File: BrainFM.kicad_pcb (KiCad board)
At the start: 2 copper layers, 21 x 34.3 mm, 18 parts, among them J1 USB_B_Micro, U1 PAM8302AAD, U2 MCP73831-2-OT, U3 TLV75801PDBV

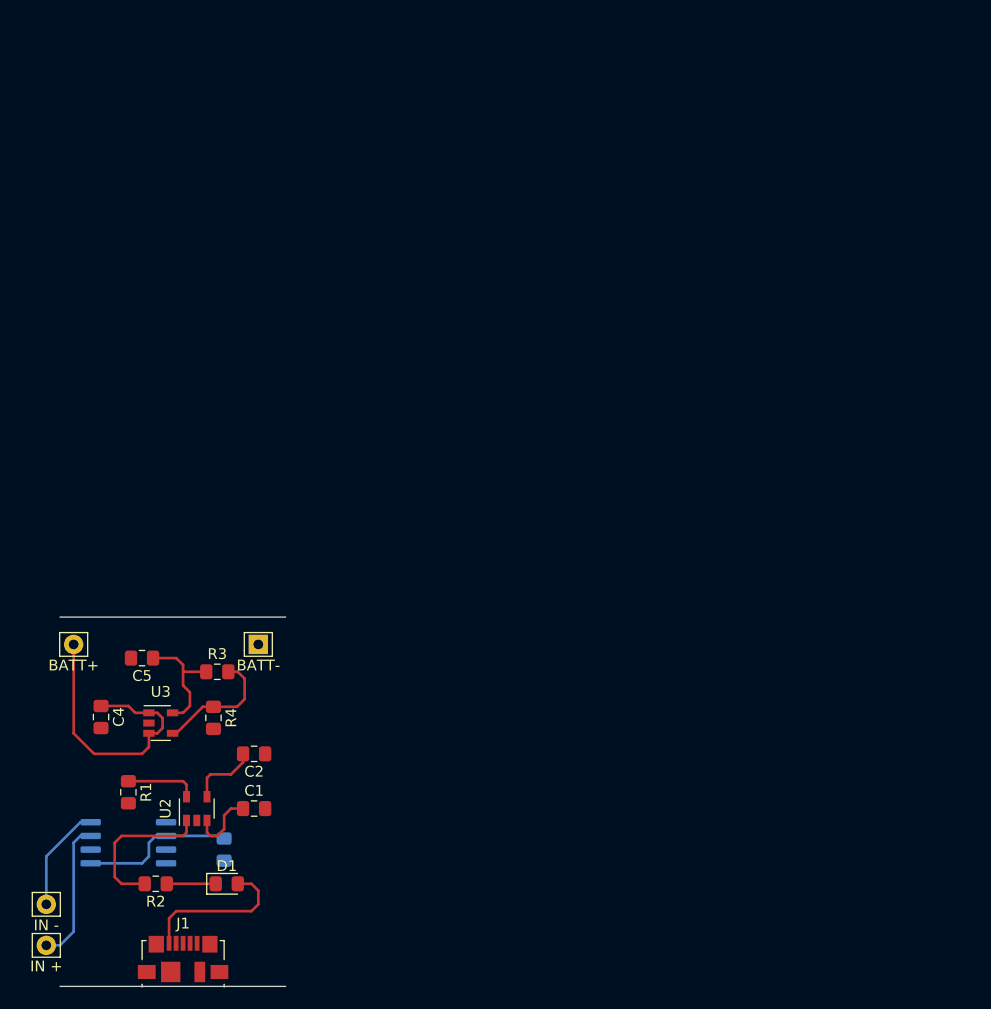
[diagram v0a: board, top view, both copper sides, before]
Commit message: update schematic and layout
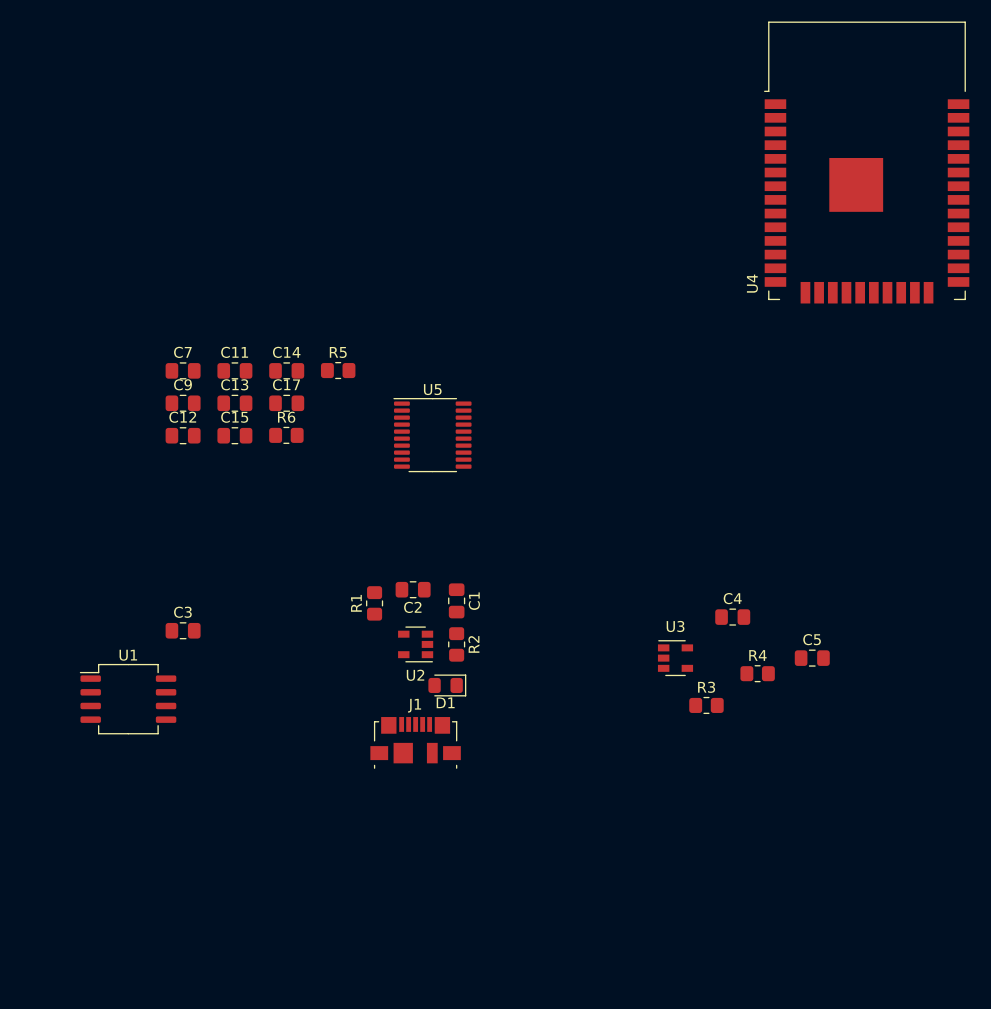
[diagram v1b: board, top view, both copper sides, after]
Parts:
- removed BATT+, BATT-: Pin_D0.9mm_L10.0mm_W2.4mm_FlatFork, Connector_Pin:Pin_D0.9mm_L10.0mm_W2.4mm_FlatFork
- removed IN +: Pin_D0.9mm_L10.0mm_W2.4mm_FlatFork, Connector_Pin:Pin_D0.9mm_L10.0mm_W2.4mm_FlatFork
- removed IN -: Pin_D0.9mm_L10.0mm_W2.4mm_FlatFork, Connector_Pin:Pin_D0.9mm_L10.0mm_W2.4mm_FlatFork
- added C11: .1 uf, Capacitor_SMD:C_0805_2012Metric_Pad1.18x1.45mm_HandSolder, F.Cu at (126.7, 64.8)
- added C12: 2.2 uf, Capacitor_SMD:C_0805_2012Metric_Pad1.18x1.45mm_HandSolder, F.Cu at (121.9, 70.8)
- added C13: 2.2 uf, Capacitor_SMD:C_0805_2012Metric_Pad1.18x1.45mm_HandSolder, F.Cu at (126.7, 67.8)
- added C14: 0.1 uf, Capacitor_SMD:C_0805_2012Metric_Pad1.18x1.45mm_HandSolder, F.Cu at (131.5, 64.8)
- added C15: 2.2 nf, Capacitor_SMD:C_0805_2012Metric_Pad1.18x1.45mm_HandSolder, F.Cu at (126.7, 70.8)
- added C17: 2.2 nf, Capacitor_SMD:C_0805_2012Metric_Pad1.18x1.45mm_HandSolder, F.Cu at (131.5, 67.8)
- added C7: .1 uf, Capacitor_SMD:C_0805_2012Metric_Pad1.18x1.45mm_HandSolder, F.Cu at (121.9, 64.8)
- added C9: .1 uf, Capacitor_SMD:C_0805_2012Metric_Pad1.18x1.45mm_HandSolder, F.Cu at (121.9, 67.8)
- added R5: 470, Resistor_SMD:R_0805_2012Metric_Pad1.20x1.40mm_HandSolder, F.Cu at (136.3, 64.7)
- added R6: 470, Resistor_SMD:R_0805_2012Metric_Pad1.20x1.40mm_HandSolder, F.Cu at (131.5, 70.8)
- added U4: ESP32-WROOM-32, RF_Module:ESP32-WROOM-32, F.Cu at (185.4, 48.3)
- added U5: PCM5102, Package_SO:TSSOP-20_4.4x6.5mm_P0.65mm, F.Cu at (145.1, 70.7)
- C1, C2, C4, C5: footprint Capacitor_SMD:C_0805_2012Metric_Pad1.15x1.40mm_HandSolder -> Capacitor_SMD:C_0805_2012Metric_Pad1.18x1.45mm_HandSolder
- C3: footprint Capacitor_SMD:C_0805_2012Metric_Pad1.15x1.40mm_HandSolder -> Capacitor_SMD:C_0805_2012Metric_Pad1.18x1.45mm_HandSolder; moved to F.Cu
- R1, R2: footprint Resistor_SMD:R_0805_2012Metric_Pad1.15x1.40mm_HandSolder -> Resistor_SMD:R_0805_2012Metric_Pad1.20x1.40mm_HandSolder
- R3: value R -> 10k; footprint Resistor_SMD:R_0805_2012Metric_Pad1.15x1.40mm_HandSolder -> Resistor_SMD:R_0805_2012Metric_Pad1.20x1.40mm_HandSolder
- R4: value R -> 2k; footprint Resistor_SMD:R_0805_2012Metric_Pad1.15x1.40mm_HandSolder -> Resistor_SMD:R_0805_2012Metric_Pad1.20x1.40mm_HandSolder
- U1: moved to F.Cu
- moved C5 62.2 mm to (180.3, 91.4), turned to 0 degrees
- moved C4 59.4 mm to (173.0, 87.6), turned to 0 degrees
- moved R4 50.7 mm to (175.3, 92.9), turned to 0 degrees
- moved U3 48.2 mm to (167.6, 91.4)
- moved R3 45.5 mm to (170.5, 95.8)
- moved R2 35.7 mm to (147.3, 90.2), turned to 270 degrees
- moved J1 29.6 mm to (143.5, 99.1)
- moved R1 28.8 mm to (139.7, 86.4), turned to 90 degrees
- moved D1 27.4 mm to (146.3, 94.0), turned to 180 degrees
- moved C1 26.9 mm to (147.3, 86.1), turned to 270 degrees
- moved U2 25.4 mm to (143.5, 90.2), turned to 180 degrees
- moved C2 21.2 mm to (143.3, 85.1)
- moved C3 20.7 mm to (121.9, 88.9), turned to 0 degrees
- moved U1 13.3 mm to (116.8, 95.2)
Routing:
- net VCC: track 26.1 -> 0.00 mm
- net +3V3: track 25.4 -> 0.00 mm
- net Net-(C2-Pad2): track 21.1 -> 0.00 mm
- net Net-(R2-Pad2): track 14.4 -> 0.00 mm
- net Net-(U1-Pad3): track 13.2 -> 0.00 mm
- net Net-(R3-Pad2): track 11.7 -> 0.00 mm
- net Net-(U1-Pad4): track 9.88 -> 0.00 mm
- net Net-(R1-Pad1): track 6.65 -> 0.00 mm
- net Net-(C1-Pad1): track 6.40 -> 0.00 mm
- net Net-(D1-Pad1): track 4.55 -> 0.00 mm
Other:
- board outline removed
